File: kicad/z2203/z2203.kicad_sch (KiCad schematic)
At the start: 46 parts, among them J1 Conn_01x01, J2 Conn_01x02, J3 Conn_02x20_Odd_Even, U15 M24C02-WMN, U3 74HC595, U4 74HC595, U5 74HC08, U6 TL074, U9 74HC04, X1 SX3M3.57

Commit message: routed z2203
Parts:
- removed C5: 0.1u, Capacitor_SMD:C_0603_1608Metric, symbol Device:C
- removed TP7: TestPoint, TestPoint:TestPoint_Pad_2.0x2.0mm, symbol Connector:TestPoint
- removed U5: 74HC08, symbol 74xx:74LS08
- removed U9: 74HC04, Package_SO:TSSOP-14_4.4x5mm_P0.65mm, symbol 74xx:74HC04
- added R9: 47k, Resistor_SMD:R_0603_1608Metric, symbol Device:R
- added TP11, TP12, TP8, TP9: TestPoint, TestPoint:TestPoint_Pad_2.0x2.0mm, symbol Connector:TestPoint
- added U7: 74HC00, Package_SO:SOIC-14_3.9x8.7mm_P1.27mm, symbol 74xx:74HC00
- R1, R56: LCSC Part (none) -> C23162
- R2, R8: LCSC C23197 -> (none); LCSC Part (none) -> C23197
- R3, R4, R5, R6, R7: LCSC Part (none) -> C25819
- U1: value ~ -> YM2203
- U2: value ~ -> YM3014; footprint (none) -> Package_DIP:DIP-8_W7.62mm
- U3, U4: footprint (none) -> Package_SO:TSSOP-16_4.4x5mm_P0.65mm; LCSC Part (none) -> C273642
- U6: footprint (none) -> Package_SO:TSSOP-14_4.4x5mm_P0.65mm; LCSC Part (none) -> C96507
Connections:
- net YM_CS is gone; now on net SPI_CS1: U1.34 (~{CS})
- net +5V: now also R1.1, U7.1, U7.14 (VCC), U7.9; no longer D1.2 (A)
- net GND: now also U6.12 (+), U6.3 (+), U7.7 (GND); no longer U6.3 (+), U6.5 (+)
- net SPI_CLK: now also U4.11 (SRCLK), U7.13
- net SPI_CS0: now also U4.12 (RCLK)
- net SPI_CS1: now also TP11.1, U7.2
- net SPI_MOSI: now also TP9.1
- net YM_A0: now also U4.7 (QH); no longer U1.40 (D0), U3.7 (QH), U4.15 (QA)
- net YM_CH_A: now also TP12.1
- net ~CLK_CS1: now reaches TP6.1
- net ~CLK_CS1: now also U3.11 (SRCLK), U7.8; no longer U4.11 (SRCLK)
- net at R3.2, R4.2, R5.2: now also U6.13 (-), R9.1; no longer U6.2 (-)
- net at R6.1: now also U6.14, R9.2; no longer U6.1
- net at R6.2, R7.1: now also U6.2 (-); no longer U6.6 (-)
- net at U2.2 (BUFF): now also U6.5 (+); no longer U6.12 (+)
- net at R7.2, R8.2: now also U6.1; no longer U6.7
- net CLK_CS1: now reaches U3.12 (RCLK)
- net CLK_CS1: now also TP8.1, U7.10, U7.11
- net at D1.1 (K): now also U4.15 (QA); no longer R1.1
- net at R1.2: now also D1.2 (A); no longer U4.7 (QH)
- net YM_A1 renamed YM_D1
- net YM_D1: now also TP3.1, U3.1 (QB); no longer U3.6 (QG)
- net YM_A2 renamed YM_D2
- net YM_D2: now also U3.2 (QC); no longer U3.5 (QF)
- net YM_A3 renamed YM_D3
- net YM_D3: now also U3.3 (QD); no longer U3.4 (QE)
- net YM_A4 renamed YM_D4
- net YM_D4: now also U3.4 (QE); no longer U3.3 (QD)
- net YM_A5 renamed YM_D5
- net YM_D5: now also U3.5 (QF); no longer U3.2 (QC)
- removed net YM_A6: TP3.1, U1.7 (D6), U3.1 (QB)
- net YM_A7 renamed YM_D0
- net YM_D0: now also U1.40 (D0); no longer U1.8 (D7)
- new net: R2.2, U6.6 (-), U6.7
- new net: U7.12, U7.3
- new net YM_D6: U1.7 (D6), U3.6 (QG)
- new net YM_D7: U1.8 (D7), U3.7 (QH)
- no-connect marks 45 -> 41
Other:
- note added: "Elim glue logic- just use CS0 and CLK then move CS1 logic to NAND eliminate one chip"
- title: Zoxnoxious 3340 Oscillator -> Zoxnoxious 2203 FM Operator Type-N (OPN)
- moved on the sheet: C1, C10, C2, C3, C37, C4, C6, C7, C8, C9, D1, D4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

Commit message: routed z2203
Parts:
- renumbered C3 to C10, C6 to C3, C10 to C4, C4 to C5, C9 to C6, C8 to C7, C7 to C8, C37 to C9, D4 to D1, D1 to D2, H4 to H1, H1 to H4, R56 to R1, R20 to R10, R1 to R11, R3 to R2, R8 to R3, R9 to R4, R4 to R5, R2 to R6, R5 to R8, R6 to R9, TP3 to TP1, TP9 to TP10, TP12 to TP2, TP11 to TP3, TP8 to TP4, TP1 to TP5, TP2 to TP6, TP6 to TP7, TP4 to TP8, TP5 to TP9, U7 to U3, U3 to U4, U6 to U5, U15 to U6, U4 to U7

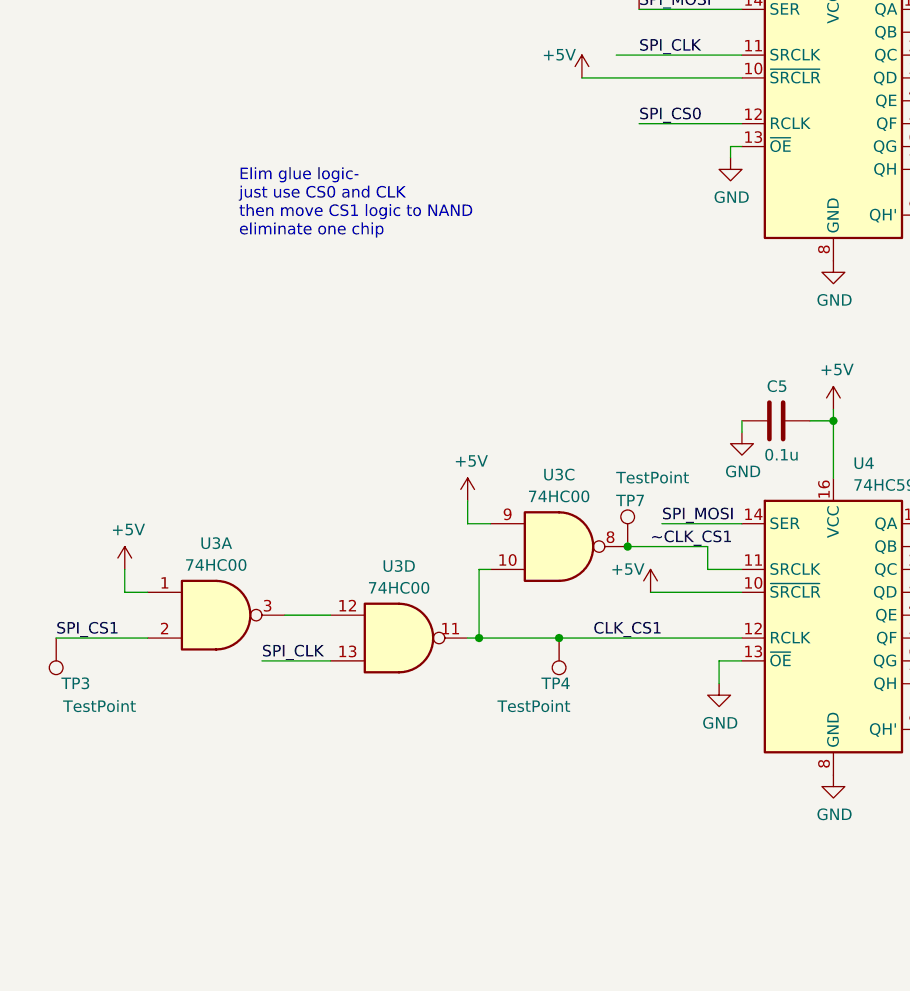
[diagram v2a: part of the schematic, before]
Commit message: move some stuff around for some minor changes.  The 2203 WR looks fine based on Capcom's Commando schematics
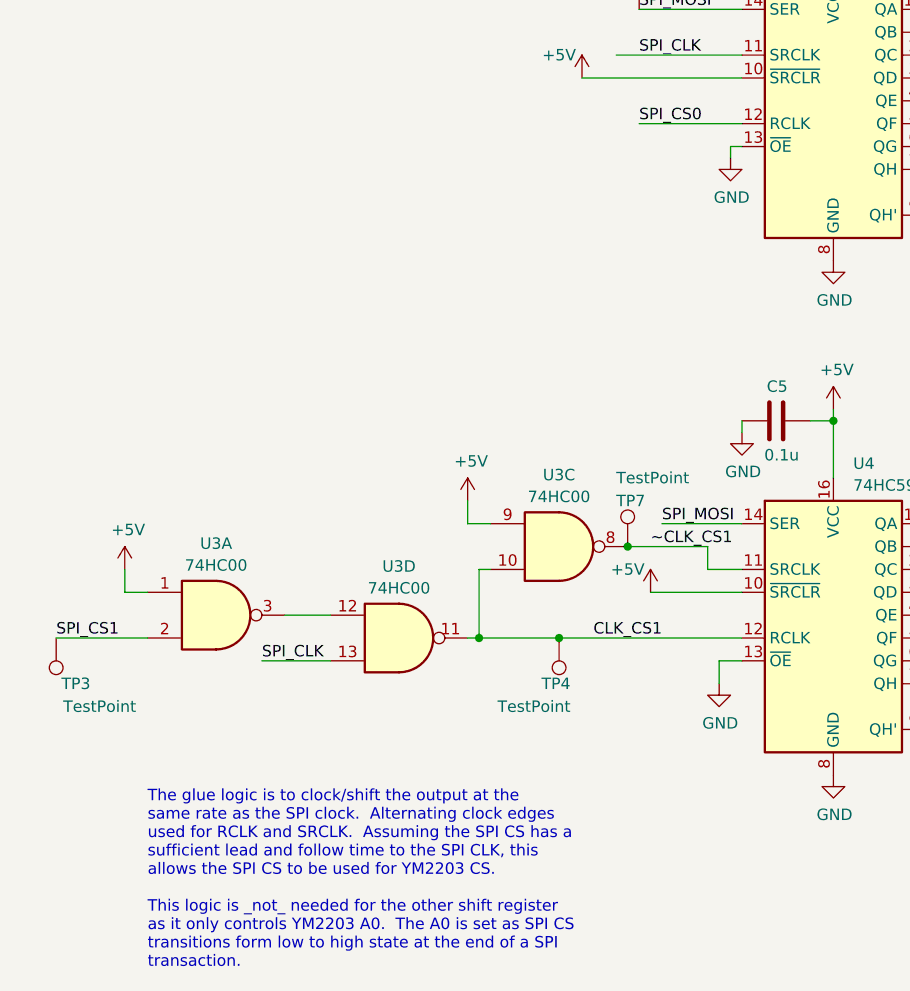
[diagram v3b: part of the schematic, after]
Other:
- note added: "The glue logic is to clock/shift the output at the same rate as the SPI clock. Alternating clock edges used for RCLK and SRCLK. Assuming the SPI CS has a sufficient lead and follow time to the SPI CLK, this allows the SPI CS to be used for YM2203 CS. This logic is _not_ needed for the other shift register as it only controls YM2203 A0. The A0 is set as SPI CS transitions form low to high state at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"
- note removed: "Elim glue logic- just use CS0 and CLK then move CS1 logic to NAND eliminate one chip"
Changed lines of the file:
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@@
     (fill (type none))
   )
-  (text "Elim glue logic-\njust use CS0 and CLK\nthen move CS1 logic to NAND\neliminate one chip"
-    (at 38.1 172.72 0)
+  (text "The glue logic is to clock/shift the output at the\nsame rate as the SPI clock.  Alternating clock edges\nused for RCLK and SRCLK.  Assuming the SPI CS has a\nsufficient lead and follow time to the SPI CLK, this\nallows the SPI CS to be used for YM2203 CS.\n\nThis logic is _not_ needed for the other shift register\nas it only controls YM2203 A0.  The A0 is set as SPI CS\ntransitions form low to high state at the end of a SPI\ntransaction."
+    (at 27.94 254 0)
     (effects (font (size 1.27 1.27)) (justify left bottom))
   )

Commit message: silkscreen updates
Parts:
- C1, C10, C2, C3, C4, C5, C7, C8, C9: LCSC (none) -> C14663; LCSC Part C14663 -> (none)
- C6: LCSC (none) -> C15850; LCSC Part C15850 -> (none)
- D1, D2: LCSC (none) -> C2286; LCSC Part C2286 -> (none)
- H1, H2, H3, H4: now left out of the parts list
- R1, R11: LCSC (none) -> C23162; LCSC Part C23162 -> (none)
- R10: LCSC (none) -> C23186; LCSC Part C23186 -> (none)
- R2, R4, R5, R7, R8, R9: LCSC (none) -> C25819; LCSC Part C25819 -> (none)
- R3, R6: LCSC (none) -> C23197; LCSC Part C23197 -> (none)
- U3: LCSC (none) -> C10090; LCSC Part C10090 -> (none)
- U4, U7: LCSC (none) -> C273642; LCSC Part C273642 -> (none)
- U5: LCSC (none) -> C96507; LCSC Part C96507 -> (none)
- U6: LCSC (none) -> C7562; LCSC Part C7562 -> (none)
- X1: LCSC (none) -> C41361373; LCSC Part C41361373 -> (none)
